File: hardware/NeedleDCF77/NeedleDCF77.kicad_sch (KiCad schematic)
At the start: 78 parts, among them J1 USB_C_Receptacle_USB2.0

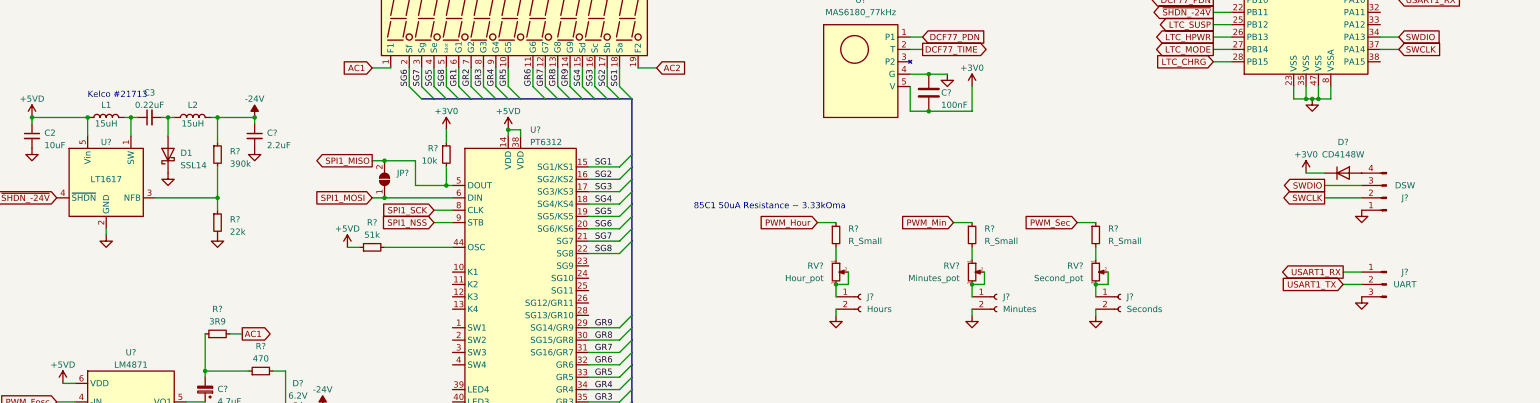
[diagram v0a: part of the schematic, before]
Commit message: Add push button for date show
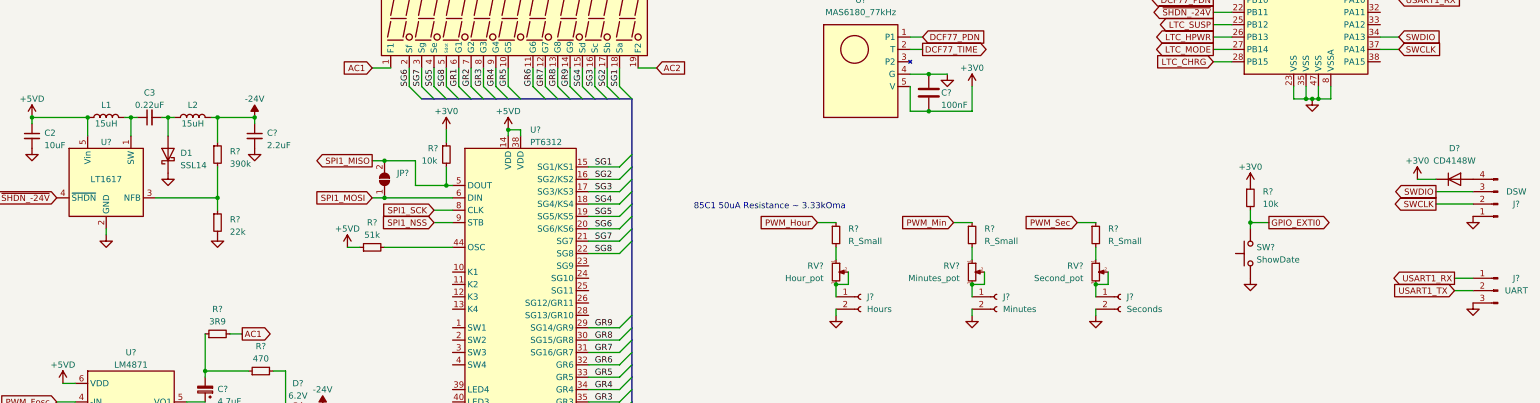
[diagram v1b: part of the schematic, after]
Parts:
- added R?: 10k, symbol Device:R_Small
- added SW?: ShowDate, symbol Switch:SW_Push
- L1: Keloc (none) -> #21713
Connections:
- net +3V0: now also R?.1
- net GND: now also SW?.1
- net GPIO_EXTI0: now also R?.2, SW?.2
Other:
- note removed: "Kelco #21713"
- moved on the sheet: D?, J?

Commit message: Add footprints and supplier codes - AMEND TO THIS
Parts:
- removed C1: 1uF, symbol Device:C_Polarized_Small
- removed C? (x2): 20pF, symbol Device:C_Small
- removed C? (x3): 10pF, symbol Device:C_Small
- removed C?: C_Small, symbol Device:C_Small
- removed C? (x3): 100nF, symbol Device:C
- removed C?: 2.2uF, symbol Device:C_Small
- removed C?: 4.7uF, symbol Device:C_Polarized
- removed R?: 10k, symbol Device:R_Small
- removed R?: 820k, symbol Device:R_Small
- removed R?: 300k, symbol Device:R_Small
- added C1, C19, C24, C5, C6: 100nF, Capacitor_SMD:C_0805_2012Metric_Pad1.18x1.45mm_HandSolder, symbol Device:C_Small
- added C12, C13, C15, C18, C8: 10pF, Capacitor_SMD:C_0805_2012Metric_Pad1.18x1.45mm_HandSolder, symbol Device:C_Small
- added C16: 4.7uF, Capacitor_SMD:CP_Elec_4x5.7, symbol Device:C_Polarized_Small
- added C20: 4.7uF, Capacitor_Tantalum_SMD:CP_EIA-3528-21_Kemet-B_Pad1.50x2.35mm_HandSolder, symbol Device:C_Polarized_Small
- added C23: 1uF, Capacitor_SMD:C_0805_2012Metric_Pad1.18x1.45mm_HandSolder, symbol Device:C_Small
- added R11: 300k, Resistor_SMD:R_0805_2012Metric_Pad1.20x1.40mm_HandSolder, symbol Device:R_Small
- added R17: 10k, Resistor_SMD:R_0805_2012Metric_Pad1.20x1.40mm_HandSolder, symbol Device:R_Small
- added R5: 820k, Resistor_SMD:R_0805_2012Metric_Pad1.20x1.40mm_HandSolder, symbol Device:R_Small
- C10, C11: renamed from C?; value 20pF -> 22pF; footprint (none) -> Capacitor_SMD:C_0805_2012Metric_Pad1.18x1.45mm_HandSolder; Kelco (none) -> #10038
- C14, C4, C7, C9: renamed from C?; footprint (none) -> Capacitor_Tantalum_SMD:CP_EIA-3216-18_Kemet-A_Pad1.58x1.35mm_HandSolder; Kelco (none) -> #15222
- C17: renamed from C?; footprint (none) -> Capacitor_SMD:C_0805_2012Metric_Pad1.18x1.45mm_HandSolder; Kelco (none) -> #7464
- C2: footprint (none) -> Capacitor_SMD:C_1206_3216Metric_Pad1.33x1.80mm_HandSolder; Kelco (none) -> #20216
- C21, C22: renamed from C?; footprint (none) -> Capacitor_SMD:CP_Elec_4x5.7; Kelco (none) -> #8457
- C3: footprint (none) -> Capacitor_SMD:C_1206_3216Metric_Pad1.33x1.80mm_HandSolder; Kelco (none) -> #12932
- D1: footprint (none) -> Diode_SMD:D_SMA_Handsoldering; uP (none) -> 054826
- D2: renamed from D?; Kelco (none) -> #8470
- D4: renamed from D?; footprint (none) -> Diode_THT:D_DO-35_SOD27_P2.54mm_Vertical_AnodeUp; Kelco (none) -> #2187
- F1: renamed from F?; value Polyfuse -> 2A; footprint (none) -> Fuse:Fuse_2512_6332Metric_Pad1.52x3.35mm_HandSolder; uP (none) -> 042637
- J1: Kelco (none) -> #20110
- J2: renamed from J?; footprint (none) -> Connector_Molex:Molex_KK-254_AE-6410-03A_1x03_P2.54mm_Vertical; Kelco (none) -> #7916
- J3: renamed from J?; footprint (none) -> Connector_PinHeader_2.54mm:PinHeader_1x04_P2.54mm_Vertical
- J4: renamed from J?; footprint (none) -> Connector_PinHeader_2.54mm:PinHeader_1x03_P2.54mm_Vertical
- J5, J6, J7: renamed from J?; footprint (none) -> Connector_Molex:Molex_KK-254_AE-6410-02A_1x02_P2.54mm_Vertical; Kelco (none) -> #7914
- JP1: renamed from JP?; footprint (none) -> Jumper:SolderJumper-2_P1.3mm_Open_TrianglePad1.0x1.5mm
- L1: footprint (none) -> Inductor_SMD:L_12x12mm_H8mm; Kelco (none) -> #21713; Keloc #21713 -> (none)
- L2: footprint (none) -> Inductor_SMD:L_12x12mm_H8mm; Kelco (none) -> #21713
- L3: renamed from L?; footprint (none) -> Inductor_SMD:L_Ferrocore_DLG-0504; Kelco (none) -> #22474
- L4: renamed from L?; footprint (none) -> Inductor_SMD:L_Ferrocore_DLG-0504; Kelco (none) -> #22472
- R1, R2: renamed from R?; footprint (none) -> Resistor_SMD:R_0805_2012Metric_Pad1.20x1.40mm_HandSolder; uP (none) -> 13102
- R10: renamed from R?; footprint (none) -> Resistor_SMD:R_1206_3216Metric_Pad1.30x1.75mm_HandSolder; Kelco (none) -> #12850
- R12: renamed from R?; footprint (none) -> Resistor_SMD:R_0805_2012Metric_Pad1.20x1.40mm_HandSolder; Kelco (none) -> #22208
- R13: renamed from R?; footprint (none) -> Resistor_SMD:R_0805_2012Metric_Pad1.20x1.40mm_HandSolder; Kelco (none) -> #12867
- R14: renamed from R?; footprint (none) -> Resistor_THT:R_Axial_DIN0207_L6.3mm_D2.5mm_P2.54mm_Vertical; uP (none) -> 32060
- R15: renamed from R?; footprint (none) -> Resistor_SMD:R_0805_2012Metric_Pad1.20x1.40mm_HandSolder; Kelco (none) -> #11602
- R16: renamed from R?; footprint (none) -> Resistor_SMD:R_0805_2012Metric_Pad1.20x1.40mm_HandSolder; Kelco (none) -> #14188
- R18, R20, R21, R22: renamed from R?; footprint (none) -> Resistor_SMD:R_0805_2012Metric_Pad1.20x1.40mm_HandSolder
- R19: renamed from R?; footprint (none) -> Resistor_SMD:R_0805_2012Metric_Pad1.20x1.40mm_HandSolder; Kelco (none) -> #11079
- R23: renamed from R?; footprint (none) -> Resistor_SMD:R_0603_1608Metric_Pad0.98x0.95mm_HandSolder; Kelco (none) -> #17150
- R24, R27: renamed from R?; footprint (none) -> Resistor_SMD:R_1206_3216Metric_Pad1.30x1.75mm_HandSolder; Kelco (none) -> #20416
- R25, R26: renamed from R?; footprint (none) -> Resistor_SMD:R_0805_2012Metric_Pad1.20x1.40mm_HandSolder; Kelco (none) -> #11076
- R3, R4, R8: renamed from R?; footprint (none) -> Resistor_SMD:R_0805_2012Metric_Pad1.20x1.40mm_HandSolder; Kelco (none) -> #11081
- R6: renamed from R?; footprint (none) -> Resistor_SMD:R_0805_2012Metric_Pad1.20x1.40mm_HandSolder; Kelco (none) -> #12853
- R7: renamed from R?; footprint (none) -> Resistor_SMD:R_0805_2012Metric_Pad1.20x1.40mm_HandSolder; Kelco (none) -> #13993
- R9: renamed from R?; footprint (none) -> Resistor_SMD:R_0805_2012Metric_Pad1.20x1.40mm_HandSolder; Kelco (none) -> #10676
- RV1: renamed from RV?; footprint (none) -> Potentiometer_THT:Potentiometer_Bourns_3296Y_Vertical; Kelco (none) -> #6738
- RV2, RV3: renamed from RV?; footprint (none) -> Potentiometer_THT:Potentiometer_Bourns_3296Y_Vertical
- SW1: renamed from SW?; footprint (none) -> Connector_Molex:Molex_KK-254_AE-6410-02A_1x02_P2.54mm_Vertical; Kelco (none) -> #7914
- Y1: renamed from Y?; footprint (none) -> Crystal:Crystal_SMD_HC49-SD_HandSoldering; Kelco (none) -> #19702
- Y2: renamed from Y?; Kelco (none) -> #13076
- gave numbers to parts that had none: 8
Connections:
- net +3V0: now also C1.1, C19.1, C8.1, R17.1, R5.1
- net +5VD: now also R11.1
- net -24V: now also C20.2, C24.2
- net GND: now also C1.2, C12.1, C13.1, C16.2, C19.2, C20.1, C23.2, C24.1, C5.1, C6.1
- net SPI1_MISO: now also R17.2
- net VBUS_P: now also C5.2
- net at R7.1, U1.4 (FB1): now also C8.2, R5.2
- net at U2.3 (PC14), Y2.2: now also C12.2
- net at R15.2: now also C18.1
- net at C17.2, U1.14 (Vc2): now also C18.2
- net at C17.1, R14.1, R15.1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: now also C15.2, R11.2
- net at U2.4 (PC15), Y2.1: now also C13.2
- net at R12.2: now also C16.1
- net at U2.7 (NRST): now also C6.2
- net at R10.2: now also C15.1
- net at U6.2 (BYPASS), U6.3 (+IN): now also C23.1
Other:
- moved on the sheet: C4

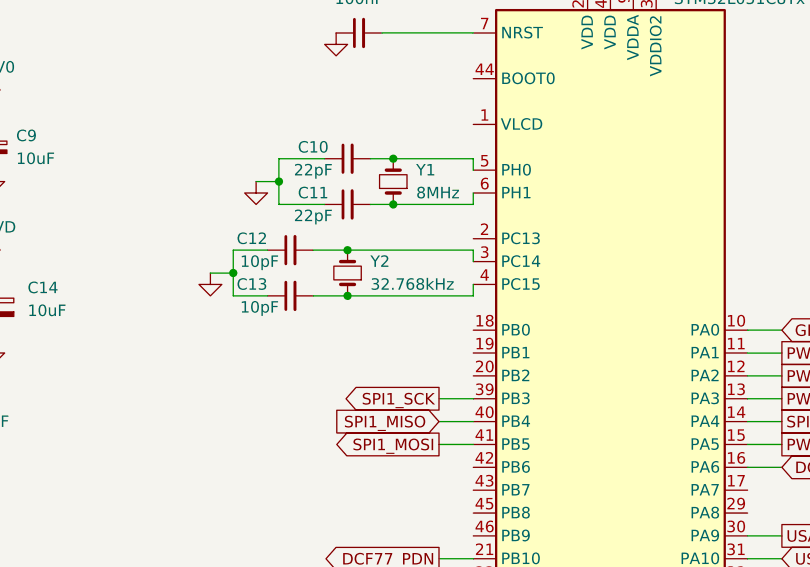
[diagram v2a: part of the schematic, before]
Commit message: Add new symbol to 32khz crystal so we can access ground
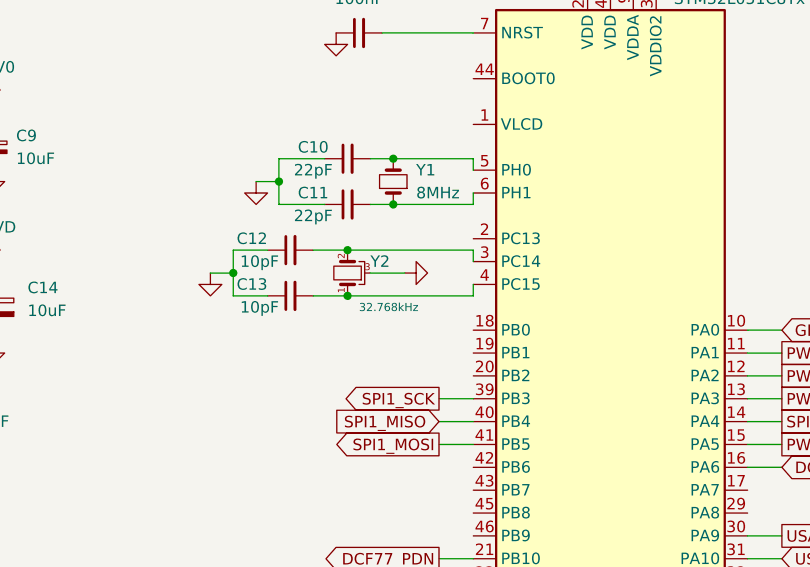
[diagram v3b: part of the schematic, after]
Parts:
- Y2: symbol Device:Crystal_Small -> Device:Crystal_GND3_Small
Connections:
- net GND: now also Y2.3
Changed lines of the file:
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@@
+    (stroke (width 0) (type default))
+  )
+  (wire (pts (xy 257.81 60.96) (xy 261.62 60.96))
     (stroke (width 0) (type default))
   )
@@
     )
   )
-  (symbol (lib_id "Device:Crystal_Small") (at 255.27 60.96 90) (unit 1)
-    (in_bom yes) (on_board yes) (dnp no) (fields_autoplaced)
+  (symbol (lib_id "Device:Crystal_GND3_Small") (at 255.27 60.96 90) (unit 1)
+    (in_bom yes) (on_board yes) (dnp no)
     (property "Reference" "Y2" (at 257.81 59.6899 90)
       (effects (font (size 1.27 1.27)) (justify right))
     )
-    (property "Value" "32.768kHz" (at 257.81 62.2299 90)
-      (effects (font (size 1.27 1.27)) (justify right))
+    (property "Value" "32.768kHz" (at 256.54 64.77 90)
+      (effects (font (size 0.9 0.9)) (justify right))
     )
     (property "Footprint" "Crystal:Crystal_C38-LF_D3.0mm_L8.0mm_Horizontal_1EP_style2" (at 255.27 60.96 0)
@@
     (pin "1")
     (pin "2")
+    (pin "3")
     (instances
       (project "NeedleDCF77"
@@
         )
       )
+    )
+  )
+  (symbol (lib_id "power:GND") (at 261.62 60.96 90) (unit 1)
+    (in_bom yes) (on_board yes) (dnp no) (fields_autoplaced)
+    (property "Reference" "#PWR031" (at 267.97 60.96 0)
+      (effects (font (size 1.27 1.27)) hide)
+    )
+    (property "Value" "GND" (at 266.7 60.96 0)
+      (effects (font (size 1.27 1.27)) hide)
+    )
+    (property "Footprint" "" (at 261.62 60.96 0)
+      (effects (font (size 1.27 1.27)) hide)
+    )
+    (property "Datasheet" "" (at 261.62 60.96 0)
+      (effects (font (size 1.27 1.27)) hide)
+    )
+    (pin "1")
+    (instances
+      (project "NeedleDCF77"
+        (path "/9538e4ed-27e6-4c37-b989-9859dc0d49e8"
+          (reference "#PWR031") (unit 1)
+        )
+      )

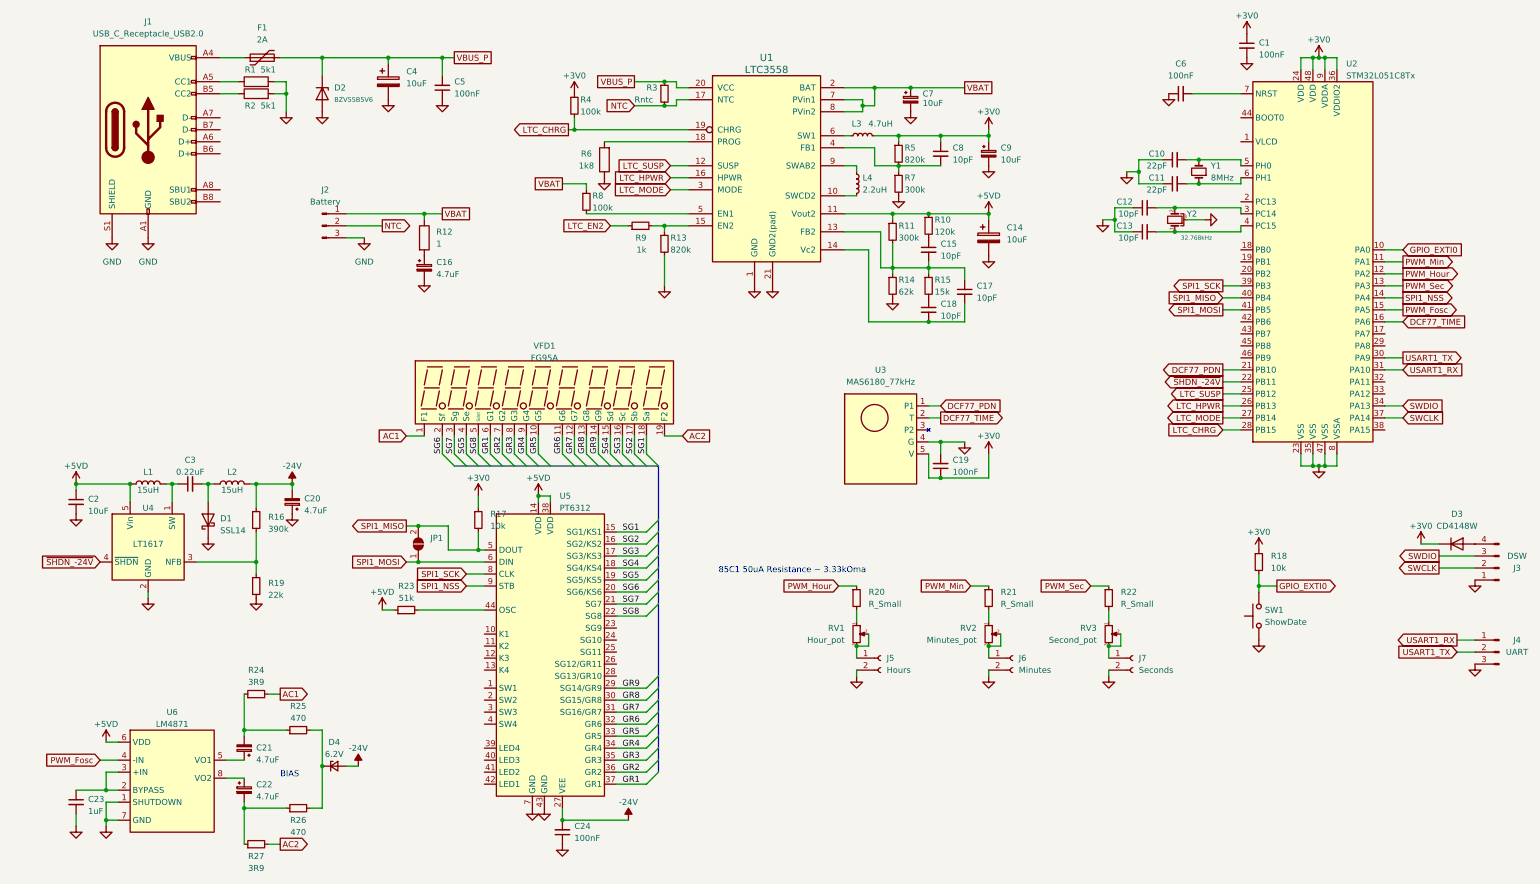
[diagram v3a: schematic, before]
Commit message: Add battery measurement circuit and generate ADC code
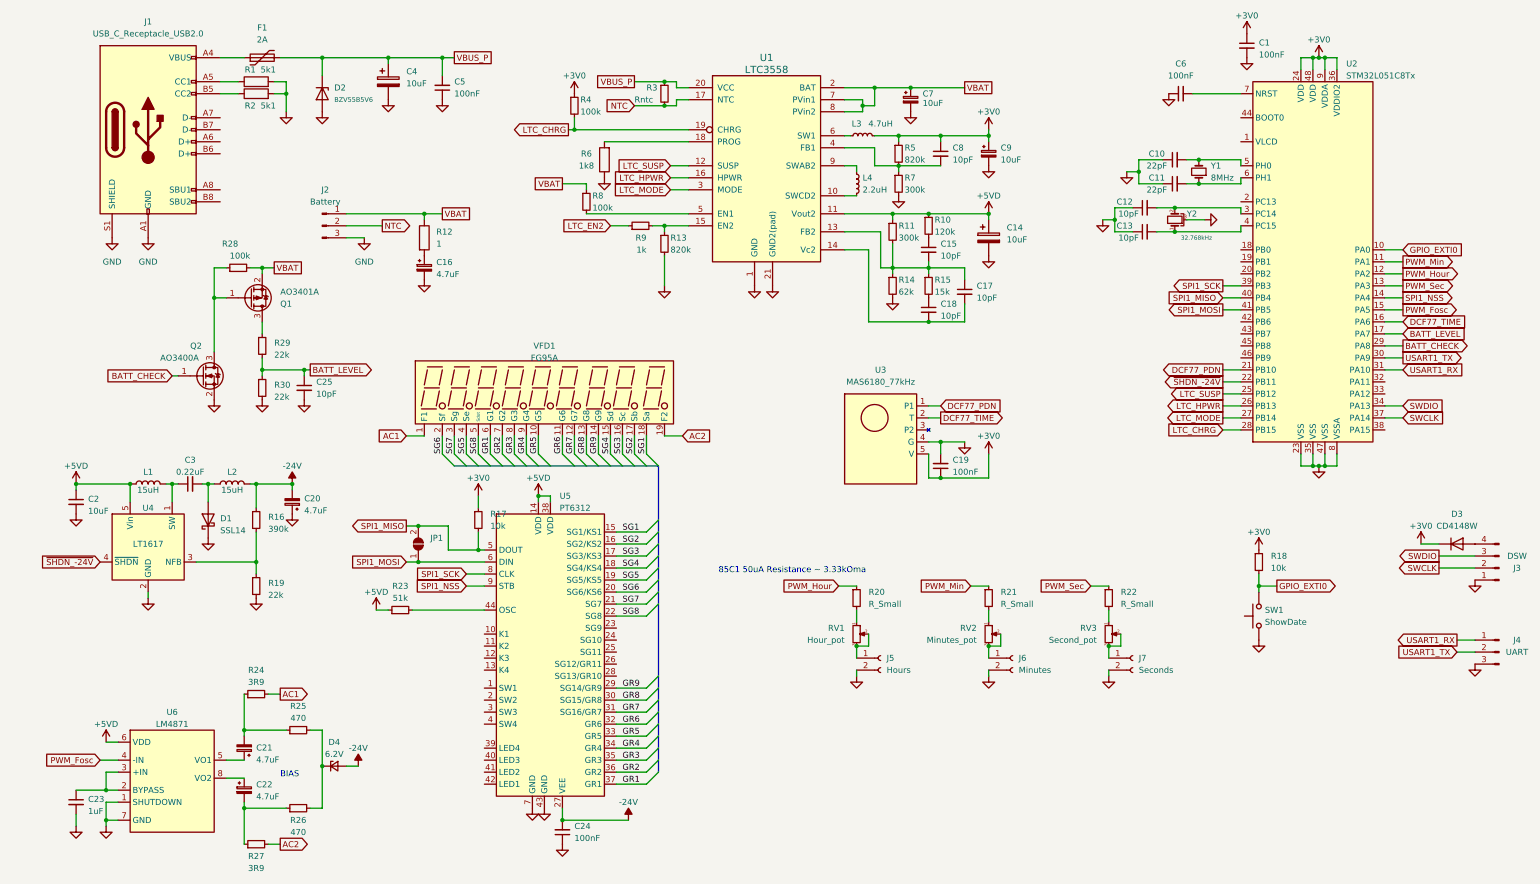
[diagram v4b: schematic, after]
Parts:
- added C25: 10pF, Capacitor_SMD:C_0805_2012Metric_Pad1.18x1.45mm_HandSolder, symbol Device:C_Small
- added Q1: AO3401A, Package_TO_SOT_SMD:SOT-23, symbol Transistor_FET:AO3401A
- added Q2: AO3400A, Package_TO_SOT_SMD:SOT-23, symbol Transistor_FET:AO3400A
- added R28: 100k, Resistor_SMD:R_0805_2012Metric_Pad1.20x1.40mm_HandSolder, symbol Device:R_Small
- added R29, R30: 22k, Resistor_SMD:R_0805_2012Metric_Pad1.20x1.40mm_HandSolder, symbol Device:R_Small
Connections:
- net GND: now also C25.2, Q2.2 (S), R30.2
- net VBAT: now also Q1.2 (S), R28.2
- net BATT_LEVEL: now reaches U2.17 (PA7)
- net BATT_LEVEL: now also C25.1, R29.2, R30.1
- net BATT_CHECK: now reaches U2.29 (PA8)
- net BATT_CHECK: now also Q2.1 (G)
- new net: Q1.1 (G), Q2.3 (D), R28.1
- new net: Q1.3 (D), R29.1
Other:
- moved on the sheet: R23
